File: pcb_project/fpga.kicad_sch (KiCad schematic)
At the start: 56 parts, among them J2 FTSH-107-01-F-DV-K, Q1 BC857BS, Q2 BC847BPN, SW1 SW_Push, U1 XC7A100T-FTG256

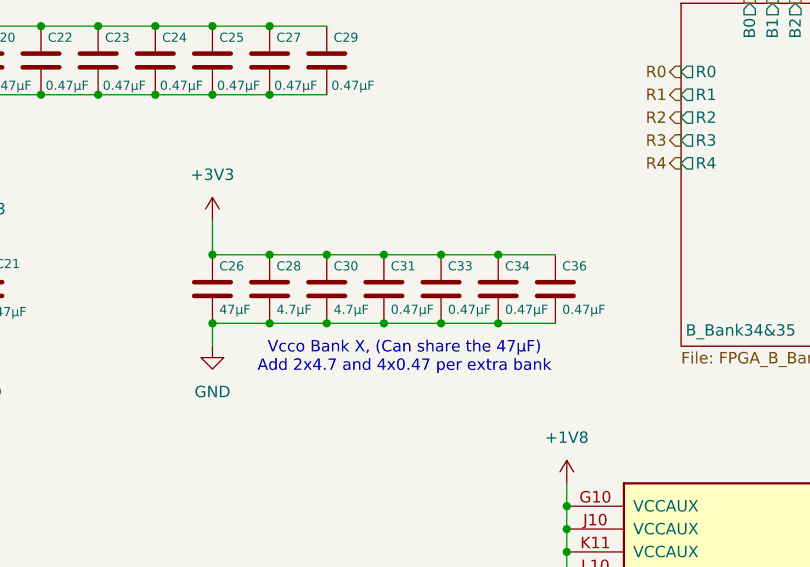
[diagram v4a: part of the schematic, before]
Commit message: Tied unused FGPA vcco to ground. Moved decoupling to all banks.
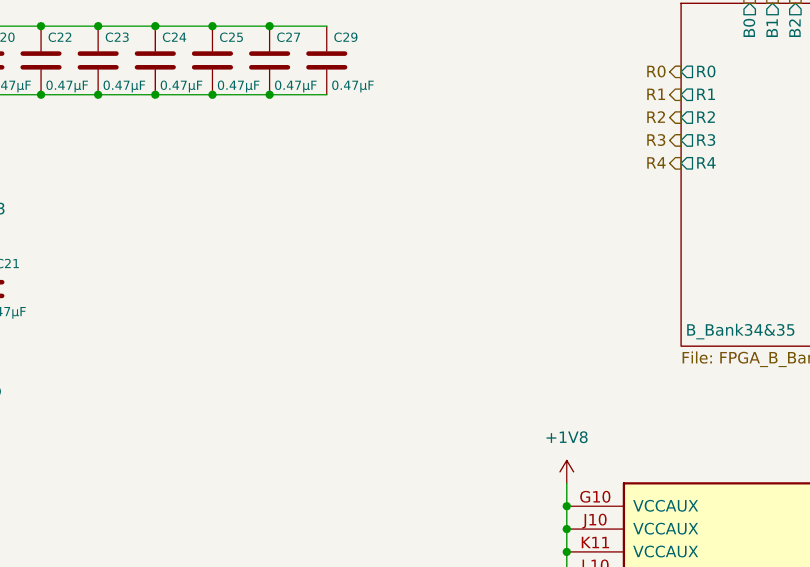
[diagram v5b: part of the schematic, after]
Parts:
- removed C26: 47µF, Capacitor_SMD:C_1210_3225Metric_Pad1.33x2.70mm_HandSolder, symbol Device:C
- removed C28, C30: 4.7µF, Capacitor_SMD:C_0805_2012Metric_Pad1.18x1.45mm_HandSolder, symbol Device:C
- removed C31, C33, C34, C36: 0.47µF, Capacitor_SMD:C_0805_2012Metric_Pad1.18x1.45mm_HandSolder, symbol Device:C
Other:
- note removed: "Vcco Bank X, (Can share the 47µF) Add 2x4.7 and 4x0.47 per extra bank"

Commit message: Add most footprints, missing some inductors and 3 buttons
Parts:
- C14: footprint (none) -> Capacitor_SMD:C_0603_1608Metric_Pad1.08x0.95mm_HandSolder
- C35: footprint (none) -> Capacitor_SMD:C_0805_2012Metric_Pad1.18x1.45mm_HandSolder
- C7: footprint (none) -> Capacitor_SMD:C_1210_3225Metric_Pad1.33x2.70mm_HandSolder
- D2, D3: footprint (none) -> LED_SMD:LED_1210_3225Metric_Pad1.42x2.65mm_HandSolder
- FB1: footprint (none) -> Inductor_SMD:L_0805_2012Metric_Pad1.15x1.40mm_HandSolder
- R13, R14, R15, R16, R17, R18, R19, R20, R21, R22, R87, R88, R89: footprint (none) -> Resistor_SMD:R_0805_2012Metric_Pad1.20x1.40mm_HandSolder
- U1: footprint (none) -> Package_BGA:Xilinx_FTG256
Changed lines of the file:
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@@
 			)
 		)
-		(property "Footprint" ""
+		(property "Footprint" "Resistor_SMD:R_0805_2012Metric_Pad1.20x1.40mm_HandSolder"
 			(at 57.912 102.87 90)
 			(effects
@@
 			)
 		)
-		(property "Footprint" ""
+		(property "Footprint" "LED_SMD:LED_1210_3225Metric_Pad1.42x2.65mm_HandSolder"
 			(at 147.32 167.64 0)
 			(effects
@@
 			)
 		)
-		(property "Footprint" ""
+		(property "Footprint" "Capacitor_SMD:C_0603_1608Metric_Pad1.08x0.95mm_HandSolder"
 			(at 126.0348 82.55 0)
 			(effects
@@
 			)
 		)
-		(property "Footprint" ""
+		(property "Footprint" "Resistor_SMD:R_0805_2012Metric_Pad1.20x1.40mm_HandSolder"
 			(at 154.178 137.16 90)
 			(effects
@@
 			)
 		)
-		(property "Footprint" ""
+		(property "Footprint" "Resistor_SMD:R_0805_2012Metric_Pad1.20x1.40mm_HandSolder"
 			(at 174.752 121.92 90)
 			(effects
@@
 			)
 		)
-		(property "Footprint" ""
+		(property "Footprint" "Package_BGA:Xilinx_FTG256"
 			(at 242.57 111.76 0)
 			(effects
@@
 			)
 		)
-		(property "Footprint" ""
+		(property "Footprint" "LED_SMD:LED_1210_3225Metric_Pad1.42x2.65mm_HandSolder"
 			(at 176.53 130.81 0)
 			(effects
@@
 			)
 		)
-		(property "Footprint" ""
+		(property "Footprint" "Resistor_SMD:R_0805_2012Metric_Pad1.20x1.40mm_HandSolder"
 			(at 131.572 137.16 90)
 			(effects
@@
 			)
 		)
-		(property "Footprint" ""
+		(property "Footprint" "Inductor_SMD:L_0805_2012Metric_Pad1.15x1.40mm_HandSolder"
 			(at 201.93 95.758 90)
 			(effects
@@
 			)
 		)
-		(property "Footprint" ""
+		(property "Footprint" "Resistor_SMD:R_0805_2012Metric_Pad1.20x1.40mm_HandSolder"
 			(at 108.712 113.03 90)
 			(effects
@@
 			)
 		)
-		(property "Footprint" ""
+		(property "Footprint" "Resistor_SMD:R_0805_2012Metric_Pad1.20x1.40mm_HandSolder"
 			(at 103.632 168.91 90)
 			(effects
@@
 			)
 		)
-		(property "Footprint" ""
+		(property "Footprint" "Resistor_SMD:R_0805_2012Metric_Pad1.20x1.40mm_HandSolder"
 			(at 137.922 171.45 90)
 			(effects
@@
 			)
 		)
-		(property "Footprint" ""
+		(property "Footprint" "Resistor_SMD:R_0805_2012Metric_Pad1.20x1.40mm_HandSolder"
 			(at 96.012 113.03 90)
 			(effects
@@
 			)
 		)
-		(property "Footprint" ""
+		(property "Footprint" "Capacitor_SMD:C_0805_2012Metric_Pad1.18x1.45mm_HandSolder"
 			(at 213.0552 106.68 0)
 			(effects
@@
 			)
 		)
-		(property "Footprint" ""
+		(property "Footprint" "Capacitor_SMD:C_1210_3225Metric_Pad1.33x2.70mm_HandSolder"
 			(at 102.5652 58.42 0)
 			(effects
@@
 			)
 		)
-		(property "Footprint" ""
+		(property "Footprint" "Resistor_SMD:R_0805_2012Metric_Pad1.20x1.40mm_HandSolder"
 			(at 149.098 158.75 90)
 			(effects
@@
 			)
 		)
-		(property "Footprint" ""
+		(property "Footprint" "Resistor_SMD:R_0805_2012Metric_Pad1.20x1.40mm_HandSolder"
 			(at 102.362 113.03 90)
 			(effects
@@
 			)
 		)
-		(property "Footprint" ""
+		(property "Footprint" "Resistor_SMD:R_0805_2012Metric_Pad1.20x1.40mm_HandSolder"
 			(at 125.222 149.86 90)
 			(effects
@@
 			)
 		)
-		(property "Footprint" ""
+		(property "Footprint" "Resistor_SMD:R_0805_2012Metric_Pad1.20x1.40mm_HandSolder"
 			(at 137.922 185.42 90)
 			(effects
@@
 			)
 		)
-		(property "Footprint" ""
+		(property "Footprint" "Package_BGA:Xilinx_FTG256"
 			(at 57.15 147.32 0)
 			(effects
@@
 			)
 		)
-		(property "Footprint" ""
+		(property "Footprint" "Resistor_SMD:R_0805_2012Metric_Pad1.20x1.40mm_HandSolder"
 			(at 162.052 147.32 90)
 			(effects

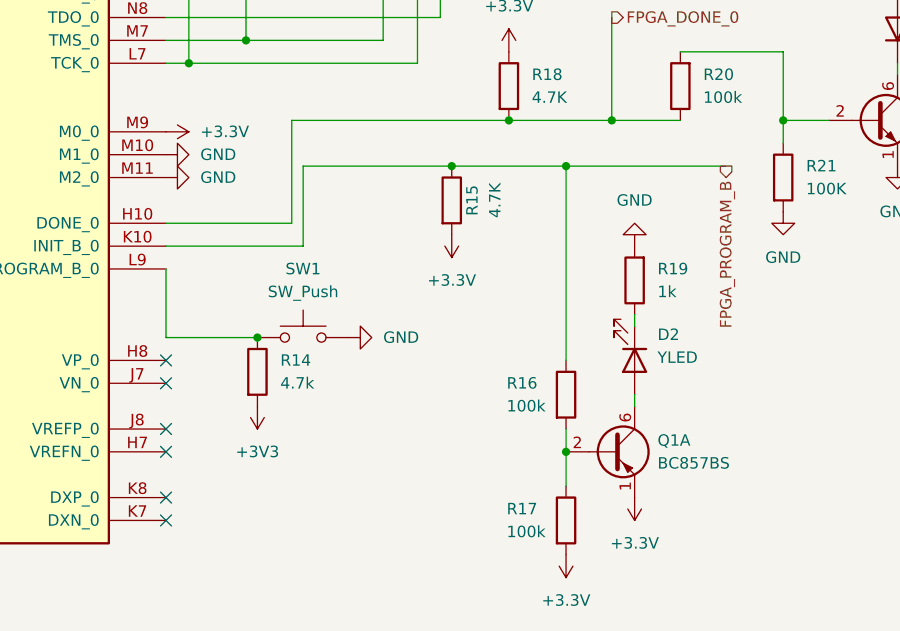
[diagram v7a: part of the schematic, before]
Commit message: Fix Program_B that was at wrong wire
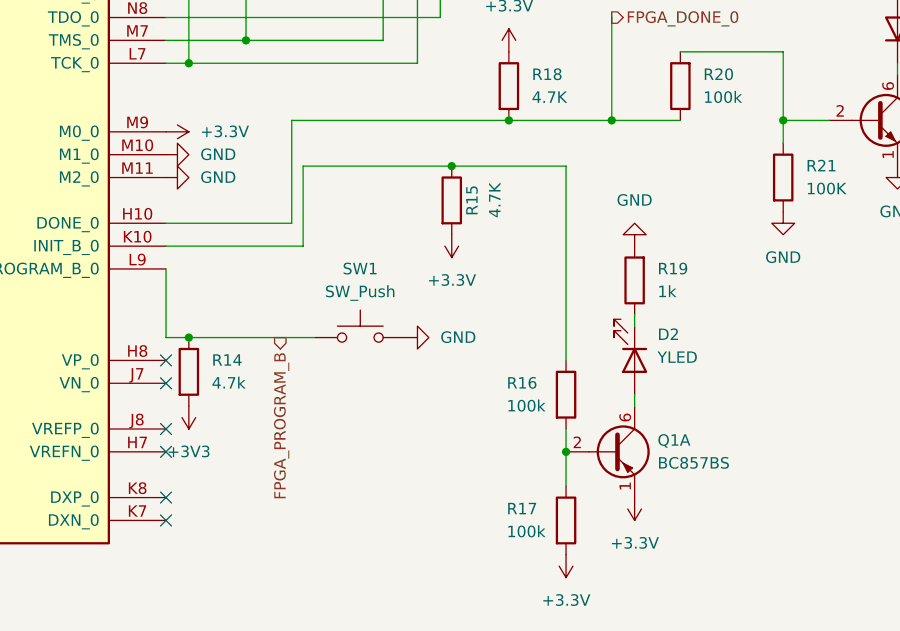
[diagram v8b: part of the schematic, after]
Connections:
- net FPGA_PROGRAM_B: now also R14.1, SW1.1, U1.L9 (PROGRAM_B_0); no longer R15.1, R16.1, U1.K10 (INIT_B_0)
- new net: R15.1, R16.1, U1.K10 (INIT_B_0)
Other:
- moved on the sheet: R14, SW1
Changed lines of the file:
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@@
 	)
 	(junction
-		(at 105.41 165.1)
-		(diameter 0)
-		(color 0 0 0 0)
-	)
-	(junction
 		(at 217.17 114.3)
 		(diameter 0)
@@
 	)
 	(junction
+		(at 97.79 165.1)
+		(diameter 0)
+		(color 0 0 0 0)
+	)
+	(junction
 		(at 104.14 106.68)
 		(diameter 0)
@@
 		(color 0 0 0 0)
 	)
-	(junction
-		(at 139.7 146.05)
-		(diameter 0)
-		(color 0 0 0 0)
-	)
 	(no_connect
 		(at 95.25 167.64)
@@
 	(wire
 		(pts
-			(xy 139.7 146.05) (xy 157.48 146.05)
-		)
-		(stroke
-			(width 0)
-			(type default)
-		)
-	)
-	(wire
-		(pts
 			(xy 125.73 105.41) (xy 125.73 129.54)
 		)
@@
 	(wire
 		(pts
-			(xy 95.25 165.1) (xy 105.41 165.1)
+			(xy 95.25 165.1) (xy 97.79 165.1)
 		)
 		(stroke
@@
 	(wire
 		(pts
+			(xy 97.79 165.1) (xy 111.76 165.1)
+		)
+		(stroke
+			(width 0)
+			(type default)
+		)
+	)
+	(wire
+		(pts
 			(xy 267.97 139.7) (xy 267.97 142.24)
 		)
@@
 	(hierarchical_label "FPGA_PROGRAM_B"
 		(shape output)
-		(at 157.48 146.05 270)
+		(at 107.95 165.1 270)
 		(effects
 			(font
@@
 	(symbol
 		(lib_id "power:+3V3")
-		(at 105.41 172.72 180)
+		(at 97.79 172.72 180)
 		(unit 1)
 		(exclude_from_sim no)
@@
 		(fields_autoplaced yes)
 		(property "Reference" "#PWR016"
-			(at 105.41 168.91 0)
+			(at 97.79 168.91 0)
 			(effects
 				(font
@@
 		)
 		(property "Value" "+3V3"
-			(at 105.41 177.8 0)
+			(at 97.79 177.8 0)
 			(effects
 				(font
@@
 		)
 		(property "Footprint" ""
-			(at 105.41 172.72 0)
+			(at 97.79 172.72 0)
 			(effects
 				(font
@@
 		)
 		(property "Datasheet" ""
-			(at 105.41 172.72 0)
+			(at 97.79 172.72 0)
 			(effects
 				(font
@@
 		)
 		(property "Description" "Power symbol creates a global label with name \"+3V3\""
-			(at 105.41 172.72 0)
+			(at 97.79 172.72 0)
 			(effects
 				(font
@@
 	(symbol
 		(lib_id "Device:R")
-		(at 105.41 168.91 0)
+		(at 97.79 168.91 0)
 		(unit 1)
 		(exclude_from_sim no)
@@
 		(fields_autoplaced yes)
 		(property "Reference" "R14"
-			(at 107.95 167.6399 0)
+			(at 100.33 167.6399 0)
 			(effects
 				(font
@@
 		)
 		(property "Value" "4.7k"
-			(at 107.95 170.1799 0)
+			(at 100.33 170.1799 0)
 			(effects
 				(font
@@
 		)
 		(property "Footprint" "Resistor_SMD:R_0805_2012Metric_Pad1.20x1.40mm_HandSolder"
-			(at 103.632 168.91 90)
+			(at 96.012 168.91 90)
 			(effects
 				(font
@@
 		)
 		(property "Datasheet" "~"
-			(at 105.41 168.91 0)
+			(at 97.79 168.91 0)
 			(effects
 				(font
@@
 		)
 		(property "Description" "Resistor"
-			(at 105.41 168.91 0)
+			(at 97.79 168.91 0)
 			(effects
 				(font
@@
 	(symbol
 		(lib_id "power:GND")
-		(at 115.57 165.1 90)
+		(at 121.92 165.1 90)
 		(unit 1)
 		(exclude_from_sim no)
@@
 		(fields_autoplaced yes)
 		(property "Reference" "#PWR018"
-			(at 121.92 165.1 0)
+			(at 128.27 165.1 0)
 			(effects
 				(font
@@
 		)
 		(property "Value" "GND"
-			(at 119.38 165.0999 90)
+			(at 125.73 165.0999 90)
 			(effects
 				(font
@@
 		)
 		(property "Footprint" ""
-			(at 115.57 165.1 0)
+			(at 121.92 165.1 0)
 			(effects
 				(font
@@
 		)
 		(property "Datasheet" ""
-			(at 115.57 165.1 0)
+			(at 121.92 165.1 0)
 			(effects
 				(font
@@
 		)
 		(property "Description" "Power symbol creates a global label with name \"GND\" , ground"
-			(at 115.57 165.1 0)
+			(at 121.92 165.1 0)
 			(effects
 				(font
@@
 	(symbol
 		(lib_id "Switch:SW_Push")
-		(at 110.49 165.1 0)
+		(at 116.84 165.1 0)
 		(unit 1)
 		(exclude_from_sim no)
@@
 		(fields_autoplaced yes)
 		(property "Reference" "SW1"
-			(at 110.49 157.48 0)
+			(at 116.84 157.48 0)
 			(effects
 				(font
@@
 		)
 		(property "Value" "SW_Push"
-			(at 110.49 160.02 0)
+			(at 116.84 160.02 0)
 			(effects
 				(font
@@
 		)
 		(property "Footprint" ""
-			(at 110.49 160.02 0)
+			(at 116.84 160.02 0)
 			(effects
 				(font
@@
 		)
 		(property "Datasheet" "~"
-			(at 110.49 160.02 0)
+			(at 116.84 160.02 0)
 			(effects
 				(font
@@
 		)
 		(property "Description" "Push button switch, generic, two pins"
-			(at 110.49 165.1 0)
+			(at 116.84 165.1 0)
 			(effects
 				(font
